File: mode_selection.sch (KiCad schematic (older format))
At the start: 38 parts, among them J1 MODE, J2 MG950-9.5, J3 MG950-9.5, J4 MG950-9.5, J5 MG950-9.5, J6 MG950-9.5, J7 PWR, K1 Fujitsu_FTR-F1C, K2 Fujitsu_FTR-F1C, K3 Fujitsu_FTR-F1C, K4 Fujitsu_FTR-F1C, Q1 BC546, Q2 BC546, Q3 BC546, Q4 BC546, U1 HEF4093B, U2 NE555, U3 LM7805_TO220, U4 7400

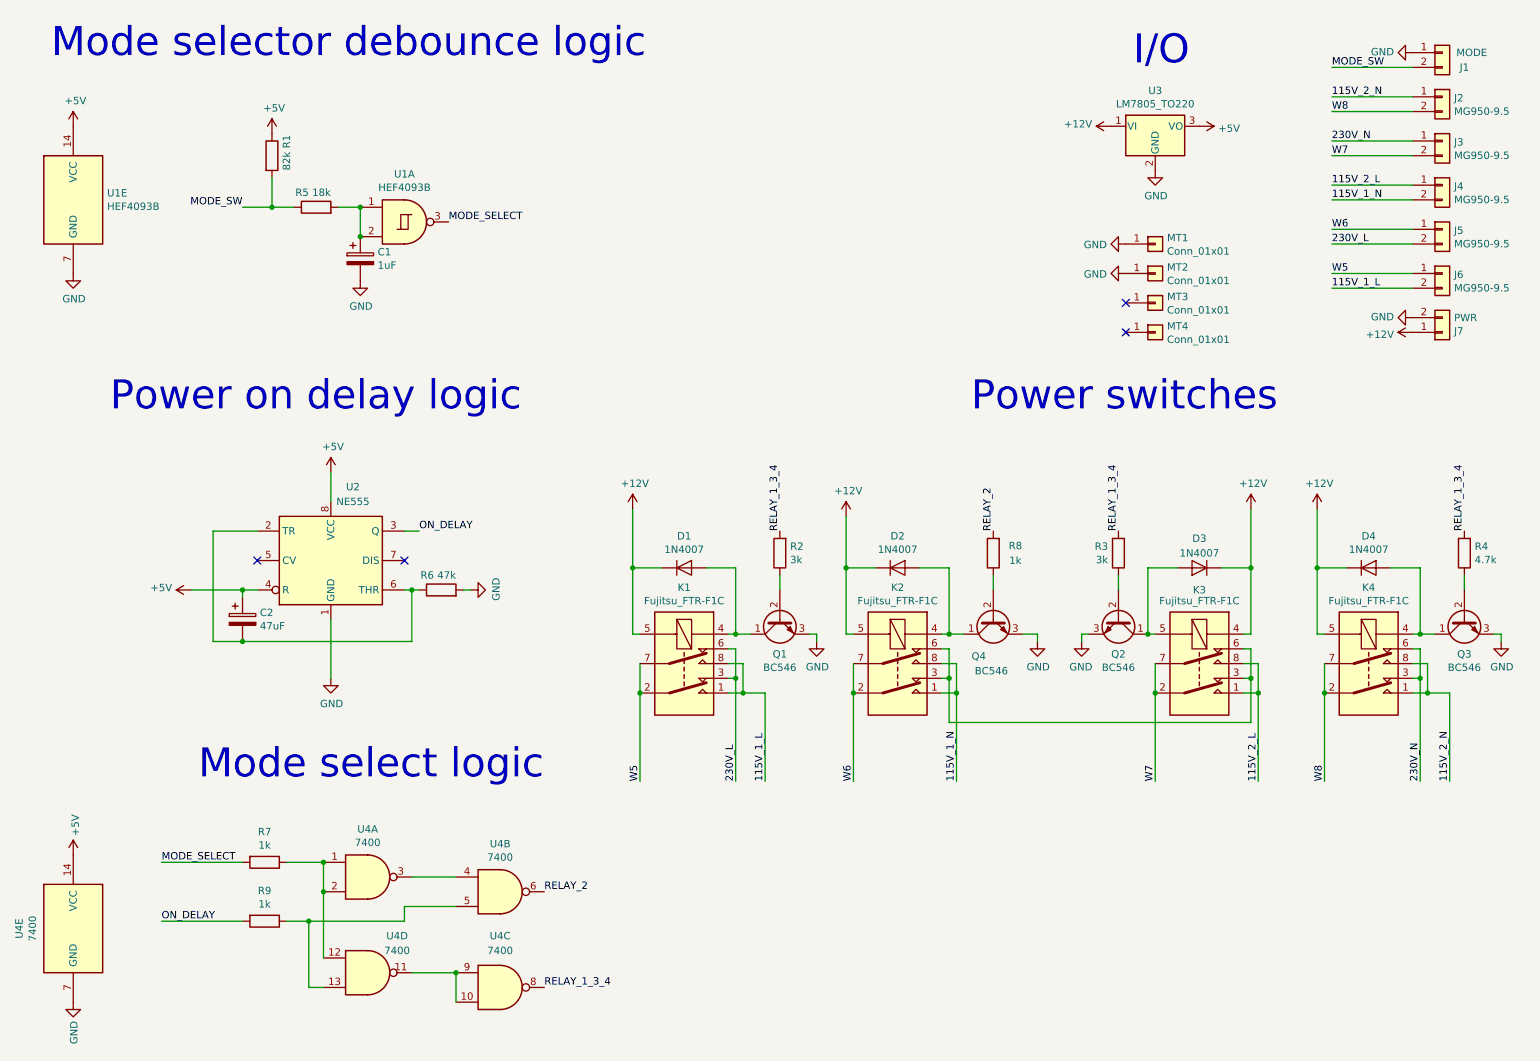
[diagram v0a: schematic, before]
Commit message: Fixes in mode selection logic
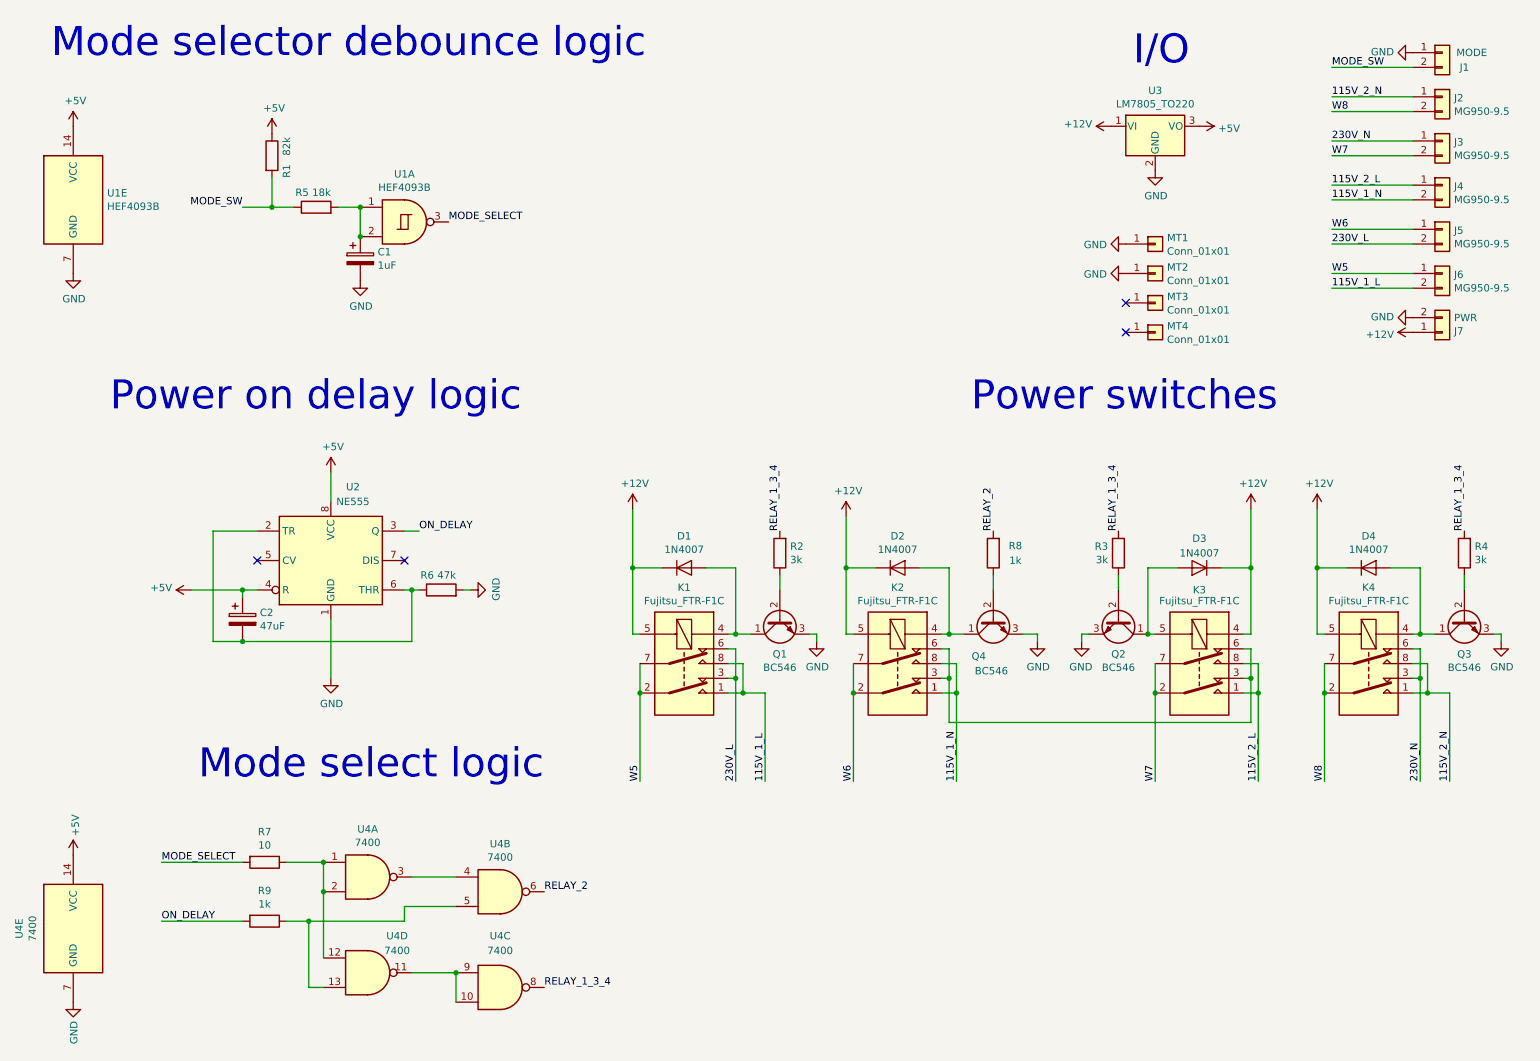
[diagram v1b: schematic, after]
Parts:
- R4: value 4.7k -> 3k
- R7: value 1k -> 10
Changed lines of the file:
@@
 P 2400 6350
 F 0 "R7" V 2193 6350 50  0000 C CNN
-F 1 "1k" V 2284 6350 50  0000 C CNN
+F 1 "10" V 2284 6350 50  0000 C CNN
 F 2 "Resistor_THT:R_Axial_DIN0207_L6.3mm_D2.5mm_P2.54mm_Vertical" V 2330 6350 50  0001 C CNN
 F 3 "~" H 2400 6350 50  0001 C CNN
@@
 U 1 1 5BFACA70
 P 2450 1550
-F 0 "R1" V 2550 1600 50  0000 L CNN
-F 1 "82k" V 2550 1450 50  0000 L CNN
+F 0 "R1" V 2550 1400 50  0000 L CNN
+F 1 "82k" V 2550 1550 50  0000 L CNN
 F 2 "Resistor_THT:R_Axial_DIN0207_L6.3mm_D2.5mm_P2.54mm_Vertical" V 2380 1550 50  0001 C CNN
 F 3 "~" H 2450 1550 50  0001 C CNN
@@
 P 10550 4250
 F 0 "R4" H 10480 4204 50  0000 R CNN
-F 1 "4.7k" H 10480 4295 50  0000 R CNN
+F 1 "3k" H 10480 4295 50  0000 R CNN
 F 2 "Resistor_THT:R_Axial_DIN0207_L6.3mm_D2.5mm_P2.54mm_Vertical" V 10480 4250 50  0001 C CNN
 F 3 "~" H 10550 4250 50  0001 C CNN

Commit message: Final schematic version
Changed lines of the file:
@@
 EESchema Schematic File Version 4
 LIBS:isolation-transformer-cache
-EELAYER 26 0
+EELAYER 30 0
 EELAYER END
 $Descr A4 11693 8268
 encoding utf-8
-Sheet 2 3
+Sheet 3 3
 Title ""
 Date ""
@@
 	1    0    0    -1
 $EndComp
-Text Label 9650 2150 0    50   ~ 0
-230V_L
-Text Label 5600 5800 1    50   ~ 0
-230V_L
 Text Label 4300 6550 0    50   ~ 0
 RELAY_2
@@
 Text Label 3450 4100 0    50   ~ 0
 ON_DELAY
-Text Label 9650 1450 0    50   ~ 0
-230V_N
-Text Label 10250 5800 1    50   ~ 0
-230V_N
-Text Label 9650 1150 0    50   ~ 0
-115V_2_N
-Text Label 10450 5800 1    50   ~ 0
-115V_2_N
-Text Label 9600 5800 1    50   ~ 0
-W8
-Text Label 9650 1250 0    50   ~ 0
-W8
-Text Label 9650 1550 0    50   ~ 0
-W7
-Text Label 9650 2050 0    50   ~ 0
-W6
-Text Label 9650 2350 0    50   ~ 0
-W5
-Text Label 8450 5800 1    50   ~ 0
-W7
-Text Label 6400 5800 1    50   ~ 0
-W6
-Text Label 4950 5800 1    50   ~ 0
-W5
-Text Label 9150 5800 1    50   ~ 0
-115V_2_L
-Text Label 9650 1750 0    50   ~ 0
-115V_2_L
-Text Label 7100 5800 1    50   ~ 0
-115V_1_N
-Text Label 9650 1850 0    50   ~ 0
-115V_1_N
-Text Label 5800 5800 1    50   ~ 0
-115V_1_L
-Text Label 9650 2450 0    50   ~ 0
-115V_1_L
 $Comp
 L power:GND #PWR0124
@@
 	0    1    -1   0
 $EndComp
-Text Label 9650 950  0    50   ~ 0
-MODE_SW
-Text Label 2250 1900 2    50   ~ 0
-MODE_SW
 Wire Wire Line
 	10200 950  9650 950
@@
 	0    1    1    0
 $EndComp
+Entry Wire Line
+	4950 5800 5050 5900
+Entry Wire Line
+	5600 5800 5700 5900
+Entry Wire Line
+	5800 5800 5900 5900
+Entry Wire Line
+	6400 5800 6500 5900
+Entry Wire Line
+	7100 5800 7200 5900
+Entry Wire Line
+	8450 5800 8550 5900
+Entry Wire Line
+	9150 5800 9250 5900
+Entry Wire Line
+	9600 5800 9700 5900
+Entry Wire Line
+	10250 5800 10350 5900
+Entry Wire Line
+	10450 5800 10550 5900
+Entry Wire Line
+	9550 2550 9650 2450
+Entry Wire Line
+	9550 2450 9650 2350
+Entry Wire Line
+	9550 2250 9650 2150
+Entry Wire Line
+	9550 2150 9650 2050
+Entry Wire Line
+	9550 1950 9650 1850
+Entry Wire Line
+	9550 1850 9650 1750
+Entry Wire Line
+	9550 1650 9650 1550
+Entry Wire Line
+	9550 1550 9650 1450
+Entry Wire Line
+	9550 1350 9650 1250
+Entry Wire Line
+	9550 1250 9650 1150
+Wire Bus Line
+	9550 3050 10950 3050
+Wire Bus Line
+	10950 3050 10950 5900
+Text HLabel 9650 950  0    50   Input ~ 0
+MODE_SW
+Text HLabel 2250 1900 0    50   Input ~ 0
+MODE_SW
+Text HLabel 9650 1150 0    50   Input ~ 0
+115V_2_N
+Text HLabel 9650 1250 0    50   Input ~ 0
+W8
+Text HLabel 9650 1450 0    50   Input ~ 0
+230V_N
+Text HLabel 9650 1550 0    50   Input ~ 0
+W7
+Text HLabel 9650 1750 0    50   Input ~ 0
+115V_2_L
+Text HLabel 9650 1850 0    50   Input ~ 0
+115V_1_N
+Text HLabel 9650 2050 0    50   Input ~ 0
+W6
+Text HLabel 9650 2150 0    50   Input ~ 0
+230V_L
+Text HLabel 9650 2350 0    50   Input ~ 0
+W5
+Text HLabel 9650 2450 0    50   Input ~ 0
+115V_1_L
+Text HLabel 10450 5800 1    50   Input ~ 0
+115V_2_N
+Text HLabel 10250 5800 1    50   Input ~ 0
+230V_N
+Text HLabel 9600 5800 1    50   Input ~ 0
+W8
+Text HLabel 9150 5800 1    50   Input ~ 0
+115V_2_L
+Text HLabel 8450 5800 1    50   Input ~ 0
+W7
+Text HLabel 7100 5800 1    50   Input ~ 0
+115V_1_N
+Text HLabel 6400 5800 1    50   Input ~ 0
+W6
+Text HLabel 5800 5800 1    50   Input ~ 0
+115V_1_L
+Text HLabel 5600 5800 1    50   Input ~ 0
+230V_L
+Text HLabel 4950 5800 1    50   Input ~ 0
+W5
+Wire Bus Line
+	5050 5900 10950 5900
+Wire Bus Line
+	9550 1250 9550 3050
 $EndSCHEMATC

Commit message: Actually used parts instead of generic ones
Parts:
- K1, K2, K3, K4: value Fujitsu_FTR-F1C -> G2R-1-E-12VDC; footprint Relay_THT:Relay_DPDT_Fujitsu_FTR-F1C -> CustomParts:Relay_SPDT_Omron_G2R-1-E; symbol Relay:Fujitsu_FTR-F1C -> CustomParts:Omron_G2R-1-E
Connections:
- net +12V: now also K1.8, K2.8, K3.1, K4.8; no longer K1.5, K2.5, K3.4, K4.5
- net 115V_1_L: now also K1.4, K1.5; no longer K1.1, K1.8
- net 115V_1_N: now also K2.4, K2.5; no longer K2.1, K2.8
- net 115V_2_L: now also K3.4, K3.5; no longer K3.1, K3.8
- net 115V_2_N: now also K4.4, K4.5; no longer K4.1, K4.8
- net 230V_L: now also K1.2, K1.7; no longer K1.3, K1.6
- net 230V_N: now also K4.2, K4.7; no longer K4.3, K4.6
- net W5: now also K1.3, K1.6; no longer K1.2, K1.7
- net W6: now also K2.3, K2.6; no longer K2.2, K2.7
- net W7: now also K3.3, K3.6; no longer K3.2, K3.7
- net W8: now also K4.3, K4.6; no longer K4.2, K4.7
- net at D2.2 (A), Q4.1 (C): now also K2.1; no longer K2.4
- net at D1.2 (A), Q1.1 (C): now also K1.1; no longer K1.4
- net at D3.2 (A), Q2.1 (C): now also K3.8; no longer K3.5
- net at D4.2 (A), Q3.1 (C): now also K4.1; no longer K4.4
- new net: K2.2, K2.7, K3.2, K3.7
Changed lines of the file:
@@
 	10200 1450 9650 1450
 Wire Wire Line
-	5800 5200 5800 5800
-Wire Wire Line
-	5600 5100 5600 5800
-Wire Wire Line
-	10450 5200 10450 5800
-Wire Wire Line
-	10250 5800 10250 5100
-Wire Wire Line
-	9150 5200 9150 5800
-Wire Wire Line
-	7100 5200 7100 5800
-Wire Wire Line
-	9100 5400 9100 5100
-Wire Wire Line
-	7050 5400 9100 5400
-Wire Wire Line
-	7050 5100 7050 5400
+	5800 5300 5800 5950
+Wire Wire Line
+	5600 5100 5600 5950
+Wire Wire Line
+	10450 5300 10450 5950
+Wire Wire Line
+	10250 5950 10250 5100
+Wire Wire Line
+	9150 5300 9150 5950
+Wire Wire Line
+	7100 5300 7100 5950
+Wire Wire Line
+	9100 5500 9100 5100
+Wire Wire Line
+	7050 5500 9100 5500
+Wire Wire Line
+	7050 5100 7050 5500
 Wire Wire Line
 	7650 4800 7650 4850
@@
 	6150 4850 6150 4800
 Wire Wire Line
-	10300 5200 10450 5200
+	10300 5300 10450 5300
+Wire Wire Line
+	10200 5300 10300 5300
+Connection ~ 10300 5300
+Wire Wire Line
+	10300 5200 10300 5300
 Wire Wire Line
 	10200 5200 10300 5200
-Connection ~ 10300 5200
-Wire Wire Line
-	10300 5000 10300 5200
-Wire Wire Line
-	10200 5000 10300 5000
 Wire Wire Line
 	10250 5100 10200 5100
 Connection ~ 10250 5100
 Wire Wire Line
-	10250 4900 10250 5100
-Wire Wire Line
-	10200 4900 10250 4900
+	10250 5000 10250 5100
+Wire Wire Line
+	10200 5000 10250 5000
 $Comp
 L power:+12V #PWR0115
@@
 	1    0    0    -1
 $EndComp
-Wire Wire Line
-	9600 5200 9600 5800
-Wire Wire Line
-	9600 5000 9600 5200
-Connection ~ 9600 5200
-$Comp
-L Relay:Fujitsu_FTR-F1C K4
+$Comp
+L CustomParts:Omron_G2R-1-E K4
 U 1 1 5BF83174
 P 9900 5000
-F 0 "K4" H 9900 5517 50  0000 C CNN
-F 1 "Fujitsu_FTR-F1C" H 9900 5426 50  0000 C CNN
-F 2 "Relay_THT:Relay_DPDT_Fujitsu_FTR-F1C" H 9850 4600 50  0001 C CNN
-F 3 "https://www.fujitsu.com/downloads/MICRO/fcai/relays/ftr-f1.pdf" H 9900 5250 50  0001 C CNN
+F 0 "K4" V 9350 5000 50  0000 C CNN
+F 1 "G2R-1-E-12VDC" V 9450 5000 50  0000 C CNN
+F 2 "CustomParts:Relay_SPDT_Omron_G2R-1-E" H 9850 4600 50  0001 C CNN
+F 3 "https://omronfs.omron.com/en_US/ecb/products/pdf/en-g2r.pdf" H 9900 5250 50  0001 C CNN
 	1    9900 5000
-	1    0    0    -1
-$EndComp
-Wire Wire Line
-	9150 5200 9050 5200
-Connection ~ 9150 5200
-Wire Wire Line
-	9150 5000 9150 5200
-Wire Wire Line
-	9050 5000 9150 5000
+	0    1    1    0
+$EndComp
+Wire Wire Line
+	9150 5300 9050 5300
+Connection ~ 9150 5300
+Wire Wire Line
+	9150 5200 9150 5300
+Wire Wire Line
+	9050 5200 9150 5200
 Wire Wire Line
 	9100 5100 9050 5100
 Connection ~ 9100 5100
 Wire Wire Line
-	9100 4900 9100 5100
-Wire Wire Line
-	9050 4900 9100 4900
+	9100 5000 9100 5100
+Wire Wire Line
+	9050 5000 9100 5000
 $Comp
 L power:+12V #PWR0113
@@
 $EndComp
 Wire Wire Line
-	8450 5200 8450 5800
-Wire Wire Line
-	8450 5000 8450 5200
-Connection ~ 8450 5200
-$Comp
-L Relay:Fujitsu_FTR-F1C K3
-U 1 1 5BF78C99
-P 8750 5000
-F 0 "K3" H 8750 5500 50  0000 C CNN
-F 1 "Fujitsu_FTR-F1C" H 8750 5426 50  0000 C CNN
-F 2 "Relay_THT:Relay_DPDT_Fujitsu_FTR-F1C" H 8700 4600 50  0001 C CNN
-F 3 "https://www.fujitsu.com/downloads/MICRO/fcai/relays/ftr-f1.pdf" H 8750 5250 50  0001 C CNN
-	1    8750 5000
-	1    0    0    -1
-$EndComp
-Wire Wire Line
-	7100 5200 7000 5200
-Connection ~ 7100 5200
-Wire Wire Line
-	7100 5000 7100 5200
-Wire Wire Line
-	7000 5000 7100 5000
+	7100 5300 7000 5300
+Connection ~ 7100 5300
 Wire Wire Line
 	7050 5100 7000 5100
 Connection ~ 7050 5100
 Wire Wire Line
-	7050 4900 7050 5100
-Wire Wire Line
-	7000 4900 7050 4900
-Wire Wire Line
-	5650 5200 5800 5200
-Wire Wire Line
-	5550 5200 5650 5200
-Connection ~ 5650 5200
-Wire Wire Line
-	5650 5000 5650 5200
-Wire Wire Line
-	5550 5000 5650 5000
+	7050 5000 7050 5100
+Wire Wire Line
+	7000 5000 7050 5000
+Wire Wire Line
+	5550 5300 5800 5300
+Wire Wire Line
+	5550 5200 5550 5300
 Wire Wire Line
 	5600 5100 5550 5100
 Connection ~ 5600 5100
 Wire Wire Line
-	5600 4900 5600 5100
-Wire Wire Line
-	5550 4900 5600 4900
+	5600 5000 5600 5100
+Wire Wire Line
+	5550 5000 5600 5000
 $Comp
 L power:+12V #PWR0111
@@
 	1    0    0    -1
 $EndComp
-Wire Wire Line
-	4950 5200 4950 5800
-Wire Wire Line
-	4950 5000 4950 5200
-Connection ~ 4950 5200
-$Comp
-L Relay:Fujitsu_FTR-F1C K1
+$Comp
+L CustomParts:Omron_G2R-1-E K1
 U 1 1 5BF5681F
 P 5250 5000
-F 0 "K1" H 5250 5517 50  0000 C CNN
-F 1 "Fujitsu_FTR-F1C" H 5250 5426 50  0000 C CNN
-F 2 "Relay_THT:Relay_DPDT_Fujitsu_FTR-F1C" H 5200 4600 50  0001 C CNN
-F 3 "https://www.fujitsu.com/downloads/MICRO/fcai/relays/ftr-f1.pdf" H 5250 5250 50  0001 C CNN
+F 0 "K1" V 4700 5000 50  0000 C CNN
+F 1 "G2R-1-E-12VDC" V 4800 5000 50  0000 C CNN
+F 2 "CustomParts:Relay_SPDT_Omron_G2R-1-E" H 5200 4600 50  0001 C CNN
+F 3 "https://omronfs.omron.com/en_US/ecb/products/pdf/en-g2r.pdf" H 5250 5250 50  0001 C CNN
 	1    5250 5000
-	1    0    0    -1
-$EndComp
-Wire Wire Line
-	6400 5200 6400 5800
-Wire Wire Line
-	6400 5200 6400 5000
-Connection ~ 6400 5200
-$Comp
-L Relay:Fujitsu_FTR-F1C K2
+	0    1    1    0
+$EndComp
+$Comp
+L CustomParts:Omron_G2R-1-E K2
 U 1 1 5BF56678
 P 6700 5000
-F 0 "K2" H 6700 5517 50  0000 C CNN
-F 1 "Fujitsu_FTR-F1C" H 6700 5426 50  0000 C CNN
-F 2 "Relay_THT:Relay_DPDT_Fujitsu_FTR-F1C" H 6650 4600 50  0001 C CNN
-F 3 "https://www.fujitsu.com/downloads/MICRO/fcai/relays/ftr-f1.pdf" H 6700 5250 50  0001 C CNN
+F 0 "K2" V 6150 5000 50  0000 C CNN
+F 1 "G2R-1-E-12VDC" V 6250 5000 50  0000 C CNN
+F 2 "CustomParts:Relay_SPDT_Omron_G2R-1-E" H 6650 4600 50  0001 C CNN
+F 3 "https://omronfs.omron.com/en_US/ecb/products/pdf/en-g2r.pdf" H 6700 5250 50  0001 C CNN
 	1    6700 5000
-	1    0    0    -1
+	0    1    1    0
 $EndComp
 $Comp
@@
 $EndComp
 Entry Wire Line
-	4950 5800 5050 5900
-Entry Wire Line
-	5600 5800 5700 5900
-Entry Wire Line
-	5800 5800 5900 5900
-Entry Wire Line
-	6400 5800 6500 5900
-Entry Wire Line
-	7100 5800 7200 5900
-Entry Wire Line
-	8450 5800 8550 5900
-Entry Wire Line
-	9150 5800 9250 5900
-Entry Wire Line
-	9600 5800 9700 5900
-Entry Wire Line
-	10250 5800 10350 5900
-Entry Wire Line
-	10450 5800 10550 5900
+	4950 5950 5050 6050
+Entry Wire Line
+	5600 5950 5700 6050
+Entry Wire Line
+	5800 5950 5900 6050
+Entry Wire Line
+	6400 5950 6500 6050
+Entry Wire Line
+	7100 5950 7200 6050
+Entry Wire Line
+	8450 5950 8550 6050
+Entry Wire Line
+	9150 5950 9250 6050
+Entry Wire Line
+	9600 5950 9700 6050
+Entry Wire Line
+	10250 5950 10350 6050
+Entry Wire Line
+	10450 5950 10550 6050
 Entry Wire Line
 	9550 2550 9650 2450
@@
 	9550 3050 10950 3050
 Wire Bus Line
-	10950 3050 10950 5900
+	10950 3050 10950 6050
 Text HLabel 9650 950  0    50   Input ~ 0
 MODE_SW
@@
 Text HLabel 9650 2450 0    50   Input ~ 0
 115V_1_L
-Text HLabel 10450 5800 1    50   Input ~ 0
+Text HLabel 10450 5950 1    50   Input ~ 0
 115V_2_N
-Text HLabel 10250 5800 1    50   Input ~ 0
+Text HLabel 10250 5950 1    50   Input ~ 0
 230V_N
-Text HLabel 9600 5800 1    50   Input ~ 0
+Text HLabel 9600 5950 1    50   Input ~ 0
 W8
-Text HLabel 9150 5800 1    50   Input ~ 0
+Text HLabel 9150 5950 1    50   Input ~ 0
 115V_2_L
-Text HLabel 8450 5800 1    50   Input ~ 0
+Text HLabel 8450 5950 1    50   Input ~ 0
 W7
-Text HLabel 7100 5800 1    50   Input ~ 0
+Text HLabel 7100 5950 1    50   Input ~ 0
 115V_1_N
-Text HLabel 6400 5800 1    50   Input ~ 0
+Text HLabel 6400 5950 1    50   Input ~ 0
 W6
-Text HLabel 5800 5800 1    50   Input ~ 0
+Text HLabel 5800 5950 1    50   Input ~ 0
 115V_1_L
-Text HLabel 5600 5800 1    50   Input ~ 0
+Text HLabel 5600 5950 1    50   Input ~ 0
 230V_L
-Text HLabel 4950 5800 1    50   Input ~ 0
+Text HLabel 4950 5950 1    50   Input ~ 0
 W5
+Wire Wire Line
+	4950 5200 4950 5300
+Connection ~ 4950 5300
+Wire Wire Line
+	4950 5300 4950 5950
+Connection ~ 5550 5300
+Wire Wire Line
+	6400 5200 6400 5300
+Connection ~ 6400 5300
+Wire Wire Line
+	6400 5300 6400 5950
+Wire Wire Line
+	7100 5200 7100 5300
+Wire Wire Line
+	7000 5200 7100 5200
+Wire Wire Line
+	8450 5200 8450 5300
+$Comp
+L CustomParts:Omron_G2R-1-E K3
+U 1 1 5BF78C99
+P 8750 5000
+F 0 "K3" V 8200 5000 50  0000 C CNN
+F 1 "G2R-1-E-12VDC" V 8300 5000 50  0000 C CNN
+F 2 "CustomParts:Relay_SPDT_Omron_G2R-1-E" H 8700 4600 50  0001 C CNN
+F 3 "https://omronfs.omron.com/en_US/ecb/products/pdf/en-g2r.pdf" H 8750 5250 50  0001 C CNN
+	1    8750 5000
+	0    1    1    0
+$EndComp
+Connection ~ 8450 5300
+Wire Wire Line
+	8450 5300 8450 5950
+Wire Wire Line
+	9600 5200 9600 5300
+Connection ~ 9600 5300
+Wire Wire Line
+	9600 5300 9600 5950
 Wire Bus Line
-	5050 5900 10950 5900
+	5050 6050 10950 6050
 Wire Bus Line
 	9550 1250 9550 3050

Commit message: Readme corrections, photos
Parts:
- U3: value LM7805_TO220 -> DD4012SB_5V
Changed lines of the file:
@@
 P 8450 1350
 F 0 "U3" H 8450 1592 50  0000 C CNN
-F 1 "LM7805_TO220" H 8450 1501 50  0000 C CNN
+F 1 "DD4012SB_5V" H 8450 1501 50  0000 C CNN
 F 2 "CustomParts:TO-220-3_Horizontal_TabDown_NoHole" H 8450 1575 50  0001 C CIN
 F 3 "http://www.fairchildsemi.com/ds/LM/LM7805.pdf" H 8450 1300 50  0001 C CNN
